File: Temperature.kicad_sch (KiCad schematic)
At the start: 29 parts, among them J3 Conn_01x24_Female, U1 ADS7953SBDBT, U3 LM321

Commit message: Forgot to add footprints and values + updated PCB froms schematic
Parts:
- removed R89, R91: R, symbol Device:R
- added R50 (x2): 100k, Resistor_SMD:R_0805_2012Metric_Pad1.20x1.40mm_HandSolder, symbol Device:R_US
- C61: value C -> 10uF; footprint (none) -> Capacitor_SMD:C_0805_2012Metric_Pad1.18x1.45mm_HandSolder
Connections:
- net +3.3V: now also R50.1
- net GND: now also R50.2
- net at U1.1 (GPIO2): now also R50.1
- net at U1.2 (GPIO3): now also R50.2
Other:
- moved on the sheet: C21, C22, R49, R50, U3

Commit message: submodule fixes and updte PCB
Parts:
- J3: symbol Connector:Conn_01x24_Female -> Connector:Conn_01x24_Socket
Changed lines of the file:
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@@
   )
   (symbol (lib_id "Device:R_US") (at 248.285 30.48 0) (unit 1)
-    (in_bom yes) (on_board yes) (dnp no) (fields_autoplaced)
-    (property "Reference" "R50" (at 250.825 29.845 0)
+    (in_bom yes) (on_board yes) (dnp no)
+    (property "Reference" "R50" (at 249.555 29.845 0)
       (effects (font (size 1.27 1.27)) (justify left))
     )
-    (property "Value" "100k" (at 250.825 32.385 0)
+    (property "Value" "100k" (at 249.555 32.385 0)
       (effects (font (size 1.27 1.27)) (justify left))
     )
@@
   )
   (symbol (lib_id "Device:R_US") (at 239.395 24.13 0) (unit 1)
-    (in_bom yes) (on_board yes) (dnp no) (fields_autoplaced)
-    (property "Reference" "R50" (at 241.935 23.495 0)
+    (in_bom yes) (on_board yes) (dnp no)
+    (property "Reference" "R50" (at 240.665 23.495 0)
       (effects (font (size 1.27 1.27)) (justify left))
     )
-    (property "Value" "100k" (at 241.935 26.035 0)
+    (property "Value" "100k" (at 240.665 26.035 0)
       (effects (font (size 1.27 1.27)) (justify left))
     )
@@
     )
   )
-  (symbol (lib_id "Connector:Conn_01x24_Female") (at 42.545 62.23 180) (unit 1)
+  (symbol (lib_id "Connector:Conn_01x24_Socket") (at 42.545 62.23 180) (unit 1)
     (in_bom yes) (on_board yes) (dnp no)
     (property "Reference" "J3" (at 42.545 25.4 0)
@@
       (effects (font (size 1.27 1.27)) hide)
     )
-    (property "Datasheet" "https://www.digikey.com/en/products/detail/jst-sales-america-inc/PADP-24V-1-S/1300227" (at 42.545 62.23 0)
-      (effects (font (size 1.27 1.27)) hide)
-    )
+    (property "Datasheet" "~" (at 42.545 62.23 0)
+      (effects (font (size 1.27 1.27)) hide)
+    )

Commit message: time flies when you're kicadding :(
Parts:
- C21, C22, C24, C61: footprint Capacitor_SMD:C_0805_2012Metric_Pad1.18x1.45mm_HandSolder -> Capacitor_SMD:C_0805_2012Metric
- R49, R50: footprint Resistor_SMD:R_0805_2012Metric_Pad1.20x1.40mm_HandSolder -> Resistor_SMD:R_0805_2012Metric
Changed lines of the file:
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@@
       (effects (font (size 1.27 1.27)))
     )
-    (property "Footprint" "Resistor_SMD:R_0805_2012Metric_Pad1.20x1.40mm_HandSolder" (at 187.706 101.981 90)
+    (property "Footprint" "Resistor_SMD:R_0805_2012Metric" (at 187.706 101.981 90)
       (effects (font (size 1.27 1.27)) hide)
     )
@@
       (effects (font (size 1.27 1.27)) (justify right))
     )
-    (property "Footprint" "Capacitor_SMD:C_0805_2012Metric_Pad1.18x1.45mm_HandSolder" (at 194.6148 100.965 0)
+    (property "Footprint" "Capacitor_SMD:C_0805_2012Metric" (at 194.6148 100.965 0)
       (effects (font (size 1.27 1.27)) hide)
     )
@@
       (effects (font (size 1.27 1.27)))
     )
-    (property "Footprint" "Resistor_SMD:R_0805_2012Metric_Pad1.20x1.40mm_HandSolder" (at 204.216 101.981 90)
+    (property "Footprint" "Resistor_SMD:R_0805_2012Metric" (at 204.216 101.981 90)
       (effects (font (size 1.27 1.27)) hide)
     )
@@
       (effects (font (size 1.27 1.27)) (justify left))
     )
-    (property "Footprint" "Resistor_SMD:R_0805_2012Metric_Pad1.20x1.40mm_HandSolder" (at 249.301 30.734 90)
+    (property "Footprint" "Resistor_SMD:R_0805_2012Metric" (at 249.301 30.734 90)
       (effects (font (size 1.27 1.27)) hide)
     )
@@
       (effects (font (size 1.27 1.27)) (justify right))
     )
-    (property "Footprint" "Capacitor_SMD:C_0805_2012Metric_Pad1.18x1.45mm_HandSolder" (at 153.9748 34.29 0)
+    (property "Footprint" "Capacitor_SMD:C_0805_2012Metric" (at 153.9748 34.29 0)
       (effects (font (size 1.27 1.27)) hide)
     )
@@
       (effects (font (size 1.27 1.27)) (justify left))
     )
-    (property "Footprint" "Capacitor_SMD:C_0805_2012Metric_Pad1.18x1.45mm_HandSolder" (at 261.3152 39.37 0)
+    (property "Footprint" "Capacitor_SMD:C_0805_2012Metric" (at 261.3152 39.37 0)
       (effects (font (size 1.27 1.27)) hide)
     )
@@
       (effects (font (size 1.27 1.27)) (justify left))
     )
-    (property "Footprint" "Resistor_SMD:R_0805_2012Metric_Pad1.20x1.40mm_HandSolder" (at 240.411 24.384 90)
+    (property "Footprint" "Resistor_SMD:R_0805_2012Metric" (at 240.411 24.384 90)
       (effects (font (size 1.27 1.27)) hide)
     )
@@
       (effects (font (size 1.27 1.27)) (justify right))
     )
-    (property "Footprint" "Capacitor_SMD:C_0805_2012Metric_Pad1.18x1.45mm_HandSolder" (at 153.3652 104.14 0)
+    (property "Footprint" "Capacitor_SMD:C_0805_2012Metric" (at 153.3652 104.14 0)
       (effects (font (size 1.27 1.27)) hide)
     )
@@
       (effects (font (size 1.27 1.27)) (justify right))
     )
-    (property "Footprint" "Capacitor_SMD:C_0805_2012Metric_Pad1.18x1.45mm_HandSolder" (at 163.5252 104.14 0)
+    (property "Footprint" "Capacitor_SMD:C_0805_2012Metric" (at 163.5252 104.14 0)
       (effects (font (size 1.27 1.27)) hide)
     )
@@
       (effects (font (size 1.27 1.27)) (justify right))
     )
-    (property "Footprint" "Capacitor_SMD:C_0805_2012Metric_Pad1.18x1.45mm_HandSolder" (at 212.3948 100.965 0)
-      (effects (font (size 1.27 1.27)) hide)
-    )
+    (property "Footprint" "Capacitor_SMD:C_0805_2012Metric" (at 212.3948 100.965 0)
+      (effects (font (size 1.27 1.27)) hide)
+    )

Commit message: killed all the COMMONers
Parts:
- U1: footprint Package_SO:TSSOP-38_4.4x9.7mm_P0.5mm -> Package_SO:HTSSOP-38-1EP_6.1x12.5mm_P0.65mm_EP5.2x12.5mm_Mask3.39x6.35mm
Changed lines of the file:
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@@
       (effects (font (size 1.524 1.524)))
     )
-    (property "Footprint" "Package_SO:TSSOP-38_4.4x9.7mm_P0.5mm" (at 237.49 31.75 0)
+    (property "Footprint" "Package_SO:HTSSOP-38-1EP_6.1x12.5mm_P0.65mm_EP5.2x12.5mm_Mask3.39x6.35mm" (at 237.49 31.75 0)
       (effects (font (size 1.27 1.27) italic) hide)
     )
-    (property "Datasheet" "ADS7953SBDBT" (at 237.49 31.75 0)
+    (property "Datasheet" "https://www.ti.com/lit/ds/symlink/ads7953.pdf?ts=1703323490930&ref_url=https%253A%252F%252Fwww.ti.com%252Fproduct%252FADS7953%252Fpart-details%252FADS7953SBDBT" (at 237.49 31.75 0)
       (effects (font (size 1.27 1.27) italic) hide)
     )

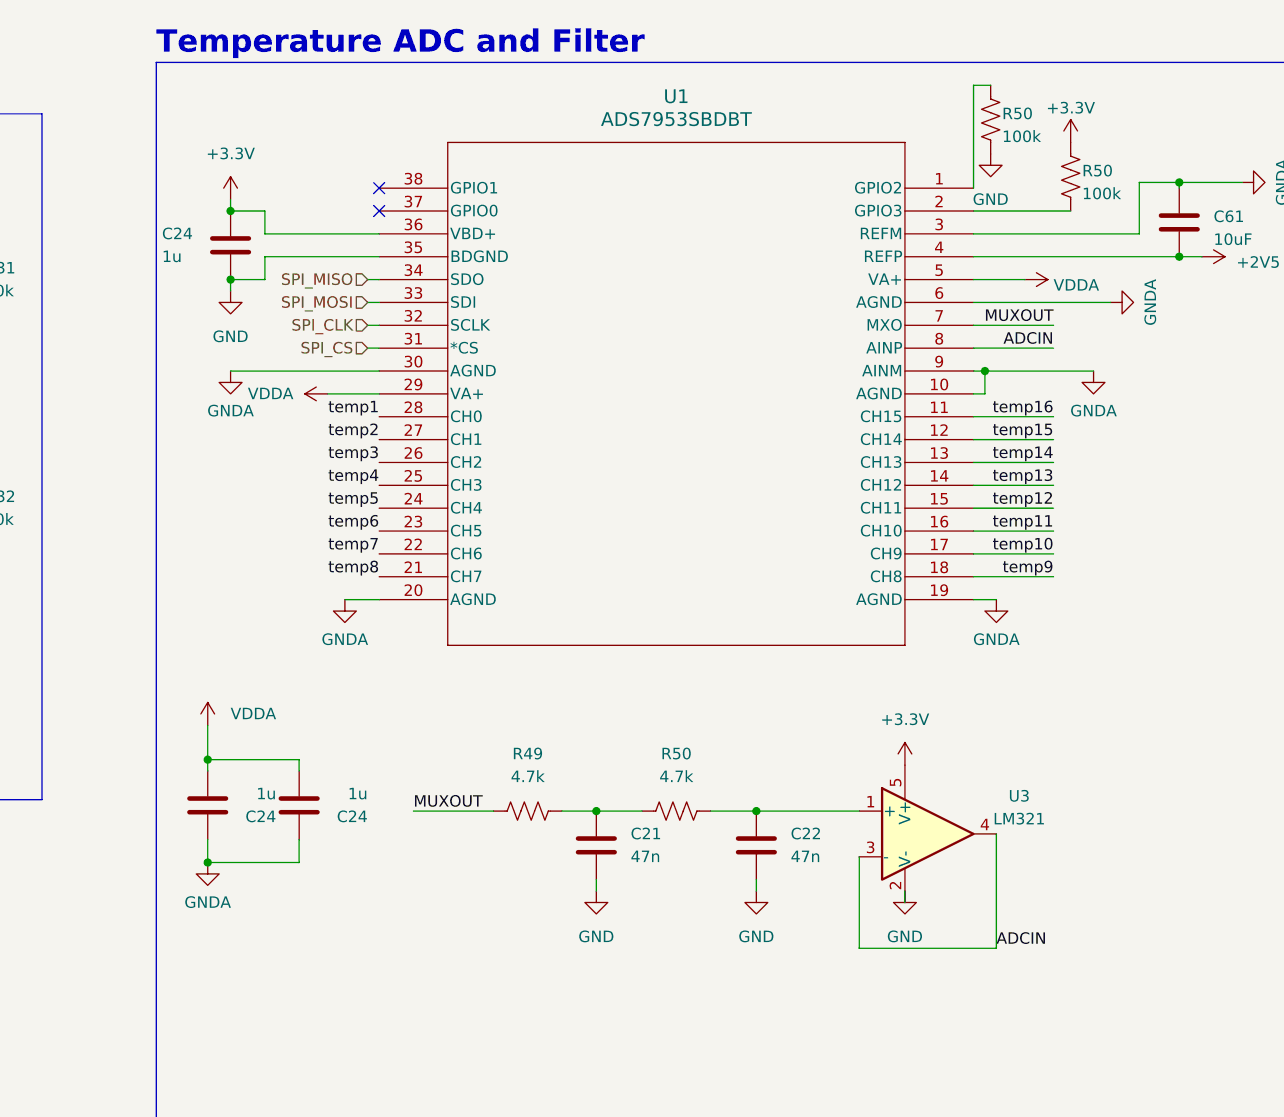
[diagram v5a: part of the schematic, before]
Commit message: new ADC layout
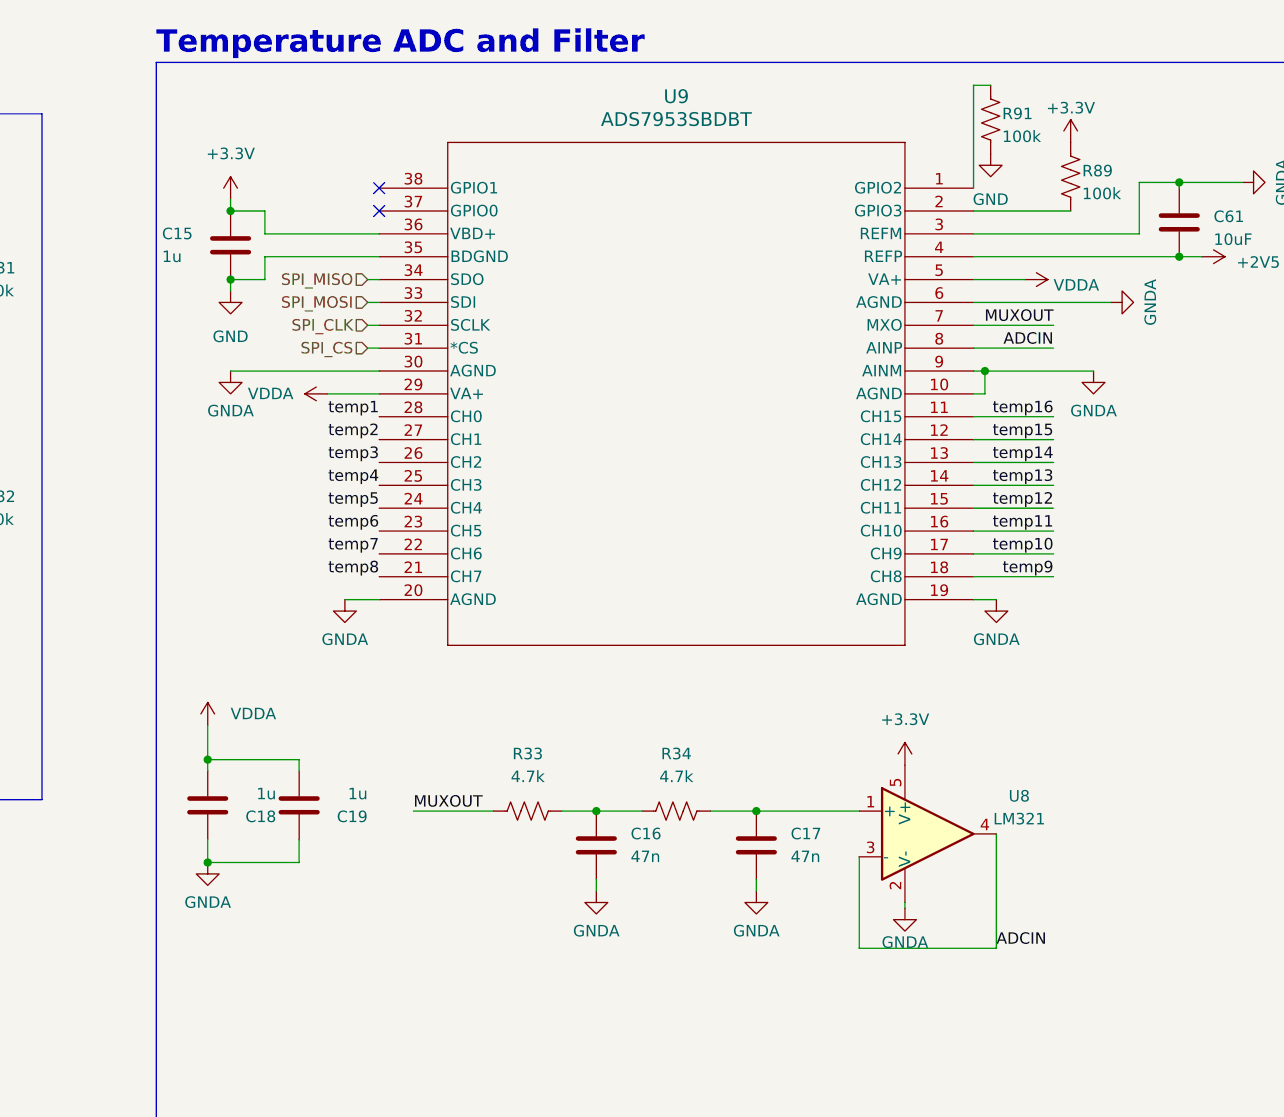
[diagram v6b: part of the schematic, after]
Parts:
- U9: renamed from U1; footprint Package_SO:HTSSOP-38-1EP_6.1x12.5mm_P0.65mm_EP5.2x12.5mm_Mask3.39x6.35mm -> Package_SO:TSSOP-38_4.4x9.7mm_P0.5mm
- renumbered C24 to C15, C21 to C16, C22 to C17, C24 to C18, C24 to C19, R49 to R33, R50 to R34, R50 to R89, R50 to R91, U3 to U8
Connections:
- net GND: no longer C16.1, C17.1, U8.2 (V-)
- net GNDA: now also C16.1, C17.1, U8.2 (V-)

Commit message: literal piss and shit
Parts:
- C15, C18, C19: value 1u -> 1uF
- C16, C17: value 47n -> 47nF
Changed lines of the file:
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@@
       (effects (font (size 1.27 1.27)) (justify right))
     )
-    (property "Value" "47n" (at 199.39 106.045 0)
+    (property "Value" "47nF" (at 199.39 106.045 0)
       (effects (font (size 1.27 1.27)) (justify right))
     )
@@
       (effects (font (size 1.27 1.27)) (justify right))
     )
-    (property "Value" "1u" (at 147.32 39.37 0)
+    (property "Value" "1uF" (at 147.32 39.37 0)
       (effects (font (size 1.27 1.27)) (justify right))
     )
@@
       (effects (font (size 1.27 1.27)) (justify right))
     )
-    (property "Value" "1u" (at 160.02 99.06 0)
+    (property "Value" "1uF" (at 160.02 99.06 0)
       (effects (font (size 1.27 1.27)) (justify right))
     )
@@
       (effects (font (size 1.27 1.27)) (justify right))
     )
-    (property "Value" "1u" (at 170.18 99.06 0)
+    (property "Value" "1uF" (at 170.18 99.06 0)
       (effects (font (size 1.27 1.27)) (justify right))
     )
@@
       (effects (font (size 1.27 1.27)) (justify right))
     )
-    (property "Value" "47n" (at 217.17 106.045 0)
-      (effects (font (size 1.27 1.27)) (justify right))
-    )
+    (property "Value" "47nF" (at 217.17 106.045 0)
+      (effects (font (size 1.27 1.27)) (justify right))
+    )

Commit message: footprint changes
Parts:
- J3: footprint UTSVT_Connectors:PADP-24V-1-S -> UTSVT_Connectors:B24B-PADSS-F
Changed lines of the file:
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@@
       (effects (font (size 1.27 1.27)))
     )
-    (property "Footprint" "UTSVT_Connectors:PADP-24V-1-S" (at 42.545 62.23 0)
+    (property "Footprint" "UTSVT_Connectors:B24B-PADSS-F" (at 42.545 62.23 0)
       (effects (font (size 1.27 1.27)) hide)
     )
